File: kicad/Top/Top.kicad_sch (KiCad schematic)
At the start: 1 part

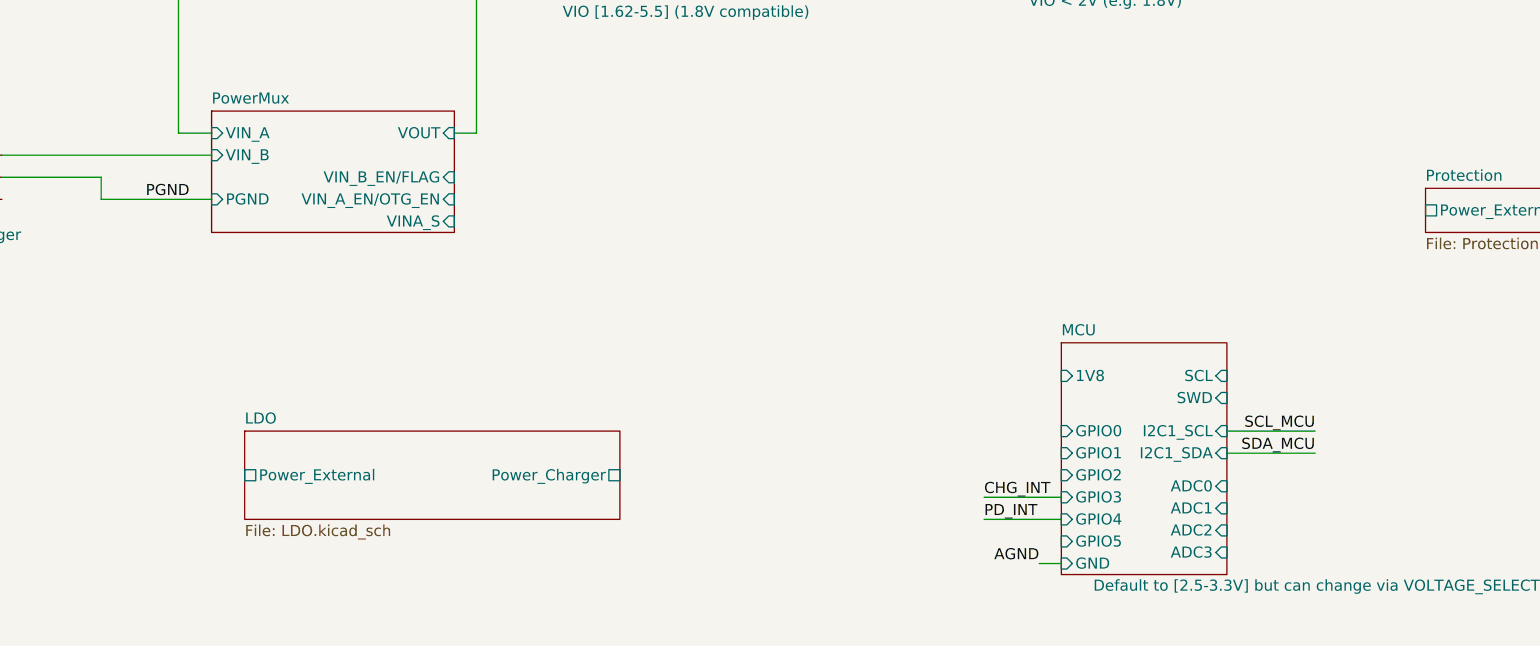
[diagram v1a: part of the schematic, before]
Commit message: Wired up power mux MCU interfaces
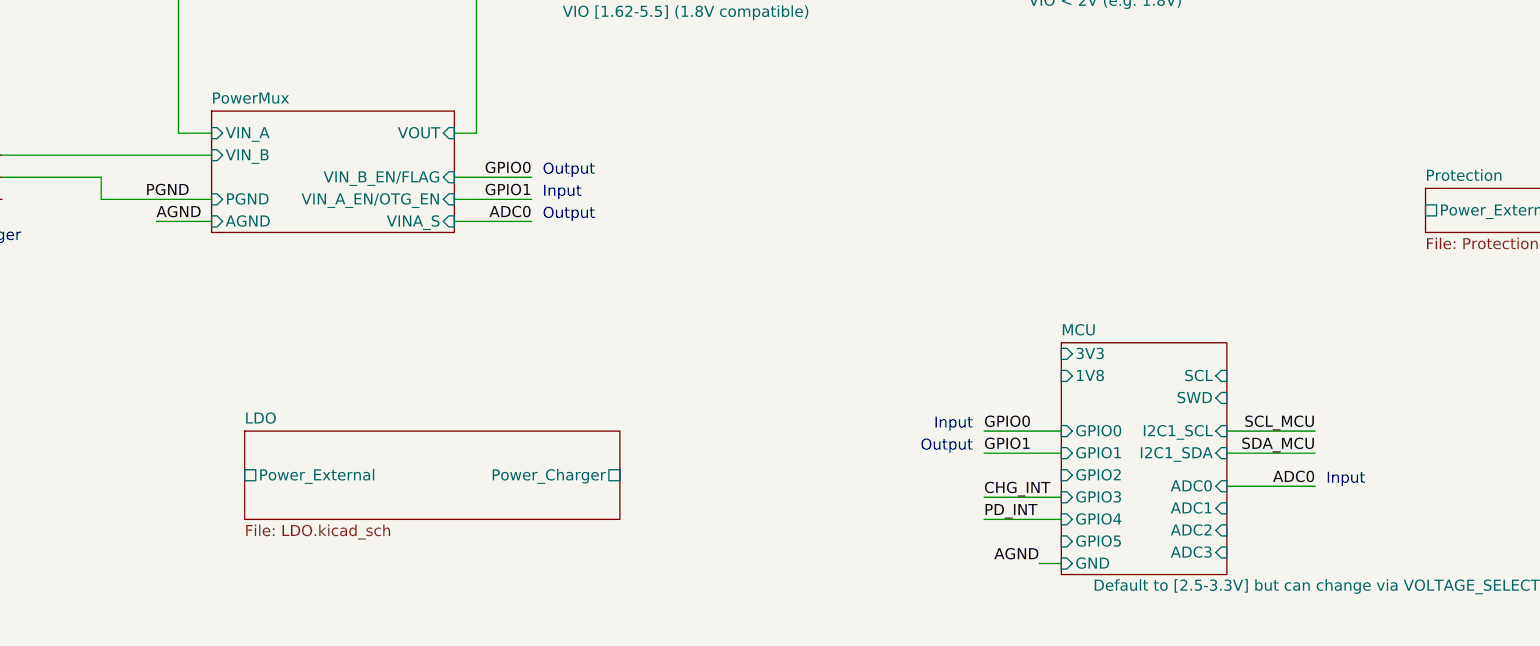
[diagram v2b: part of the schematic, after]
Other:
- sheet MCU ports: added 3V3; removed none
- sheet PowerMux ports: added AGND; removed none
- note added: "Input"
- note added: "Output"
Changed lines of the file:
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@@
+    (stroke (width 0) (type default) (color 0 0 0 0))
+  )
+  (wire (pts (xy 127 87.63) (xy 135.89 87.63))
+    (stroke (width 0) (type default) (color 0 0 0 0))
+  )
+  (wire (pts (xy 135.89 82.55) (xy 127 82.55))
+    (stroke (width 0) (type default) (color 0 0 0 0))
+  )
+  (wire (pts (xy 215.9 118.11) (xy 226.06 118.11))
     (stroke (width 0) (type default) (color 0 0 0 0))
   )
@@
     (stroke (width 0) (type default) (color 0 0 0 0))
   )
+  (wire (pts (xy 99.06 87.63) (xy 92.71 87.63))
+    (stroke (width 0) (type default) (color 0 0 0 0))
+  )
   (wire (pts (xy 160.02 48.26) (xy 168.91 48.26))
     (stroke (width 0) (type default) (color 0 0 0 0))
@@
     (stroke (width 0) (type default) (color 0 0 0 0))
   )
+  (wire (pts (xy 187.96 111.76) (xy 196.85 111.76))
+    (stroke (width 0) (type default) (color 0 0 0 0))
+  )
   (wire (pts (xy 72.39 21.59) (xy 77.47 21.59))
     (stroke (width 0) (type default) (color 0 0 0 0))
@@
     (stroke (width 0) (type default) (color 0 0 0 0))
   )
+  (wire (pts (xy 187.96 114.3) (xy 196.85 114.3))
+    (stroke (width 0) (type default) (color 0 0 0 0))
+  )
   (wire (pts (xy 129.54 77.47) (xy 129.54 34.29))
     (stroke (width 0) (type default) (color 0 0 0 0))
@@
   )
   (wire (pts (xy 185.42 40.64) (xy 191.77 40.64))
+    (stroke (width 0) (type default) (color 0 0 0 0))
+  )
+  (wire (pts (xy 135.89 85.09) (xy 127 85.09))
     (stroke (width 0) (type default) (color 0 0 0 0))
   )
@@
     (effects (font (size 1.27 1.27)) (justify left bottom))
   )
+  (text "Input" (at 186.69 111.76 180)
+    (effects (font (size 1.27 1.27)) (justify right bottom))
+  )
+  (text "Output" (at 137.16 82.55 0)
+    (effects (font (size 1.27 1.27)) (justify left bottom))
+  )
+  (text "Input" (at 137.16 85.09 0)
+    (effects (font (size 1.27 1.27)) (justify left bottom))
+  )
+  (text "Output" (at 137.16 87.63 0)
+    (effects (font (size 1.27 1.27)) (justify left bottom))
+  )
+  (text "Output" (at 186.69 114.3 180)
+    (effects (font (size 1.27 1.27)) (justify right bottom))
+  )
+  (text "Input" (at 227.33 118.11 0)
+    (effects (font (size 1.27 1.27)) (justify left bottom))
+  )
   (label "CHG_INT" (at 187.96 119.38 0)
     (effects (font (size 1.27 1.27)) (justify left bottom))
@@
     (effects (font (size 1.27 1.27)) (justify left bottom))
   )
+  (label "AGND" (at 92.71 87.63 0)
+    (effects (font (size 1.27 1.27)) (justify left bottom))
+  )
   (label "1.8V" (at 78.74 48.26 180)
     (effects (font (size 1.27 1.27)) (justify right bottom))
@@
     (effects (font (size 1.27 1.27)) (justify right bottom))
   )
+  (label "GPIO1" (at 135.89 85.09 180)
+    (effects (font (size 1.27 1.27)) (justify right bottom))
+  )
+  (label "GPIO0" (at 135.89 82.55 180)
+    (effects (font (size 1.27 1.27)) (justify right bottom))
+  )
+  (label "GPIO1" (at 187.96 114.3 0)
+    (effects (font (size 1.27 1.27)) (justify left bottom))
+  )
   (label "SDA_MCU" (at 226.06 114.3 180)
     (effects (font (size 1.27 1.27)) (justify right bottom))
@@
     (effects (font (size 1.27 1.27)) (justify right bottom))
   )
+  (label "ADC0" (at 135.89 87.63 180)
+    (effects (font (size 1.27 1.27)) (justify right bottom))
+  )
   (label "SDA_PD" (at 81.28 53.34 180)
     (effects (font (size 1.27 1.27)) (justify right bottom))
@@
   (label "AGND" (at 166.37 54.61 180)
     (effects (font (size 1.27 1.27)) (justify right bottom))
+  )
+  (label "ADC0" (at 226.06 118.11 180)
+    (effects (font (size 1.27 1.27)) (justify right bottom))
+  )
+  (label "GPIO0" (at 187.96 111.76 0)
+    (effects (font (size 1.27 1.27)) (justify left bottom))
   )
   (label "SYS" (at 77.47 21.59 180)
@@
       (effects (font (size 1.27 1.27)) (justify right))
     )
+    (pin "3V3" input (at 196.85 102.87 180)
+      (effects (font (size 1.27 1.27)) (justify left))
+    )
   )
   (sheet (at 99.06 74.93) (size 27.94 13.97) (fields_autoplaced)
@@
     (pin "VINA_S" input (at 127 87.63 0)
       (effects (font (size 1.27 1.27)) (justify right))
+    )
+    (pin "AGND" input (at 99.06 87.63 180)
+      (effects (font (size 1.27 1.27)) (justify left))
     )
   )
@@
       (reference "C?") (unit 1) (value "10uF") (footprint "")
     )
+    (path "/b17a9dbb-4562-473a-b13f-bbad723355f8/4807e2b0-3f60-4d41-a0cc-ee902e81d7ab"
+      (reference "C?") (unit 1) (value "100n") (footprint "Capacitor_SMD:C_0402_1005Metric")
+    )
     (path "/3b7e5198-fb12-4059-9002-c176f652e784/4c953f3a-dc40-4122-89b2-145f82abc098"
       (reference "C?") (unit 1) (value "0.1uF") (footprint "")
@@
       (reference "C?") (unit 1) (value "10nF") (footprint "")
     )
+    (path "/b17a9dbb-4562-473a-b13f-bbad723355f8/ea0eb13f-7d93-496c-b4f9-195da6a28f8d"
+      (reference "C?") (unit 1) (value "100n") (footprint "Capacitor_SMD:C_0402_1005Metric")
+    )
     (path "/3b7e5198-fb12-4059-9002-c176f652e784/f147c89c-1eb3-4bed-90e8-126acad15e7d"
       (reference "C?") (unit 1) (value "DNP") (footprint "")
@@
       (reference "R65") (unit 1) (value "R_SEN") (footprint "AltiumImports:1206")
     )
+    (path "/e17fda7c-211f-4188-9d42-b948f78009dd/0cea1315-6c66-4c7d-babe-09dc48335b98"
+      (reference "R?") (unit 1) (value "4.64M") (footprint "")
+    )
     (path "/b17a9dbb-4562-473a-b13f-bbad723355f8/19d6e89f-5af0-4248-ad27-14f3cf2d11c3"
       (reference "R?") (unit 1) (value "1") (footprint "")
@@
       (reference "R?") (unit 1) (value "1") (footprint "")
     )
+    (path "/e17fda7c-211f-4188-9d42-b948f78009dd/fb5ff5e7-45b6-4903-ab08-36293b183844"
+      (reference "R?") (unit 1) (value "2.61M") (footprint "")
+    )
     (path "/427922e5-a943-4728-8788-709c0c3b2395/5348c353-2ef7-4ba8-ba47-d79055695ce1"

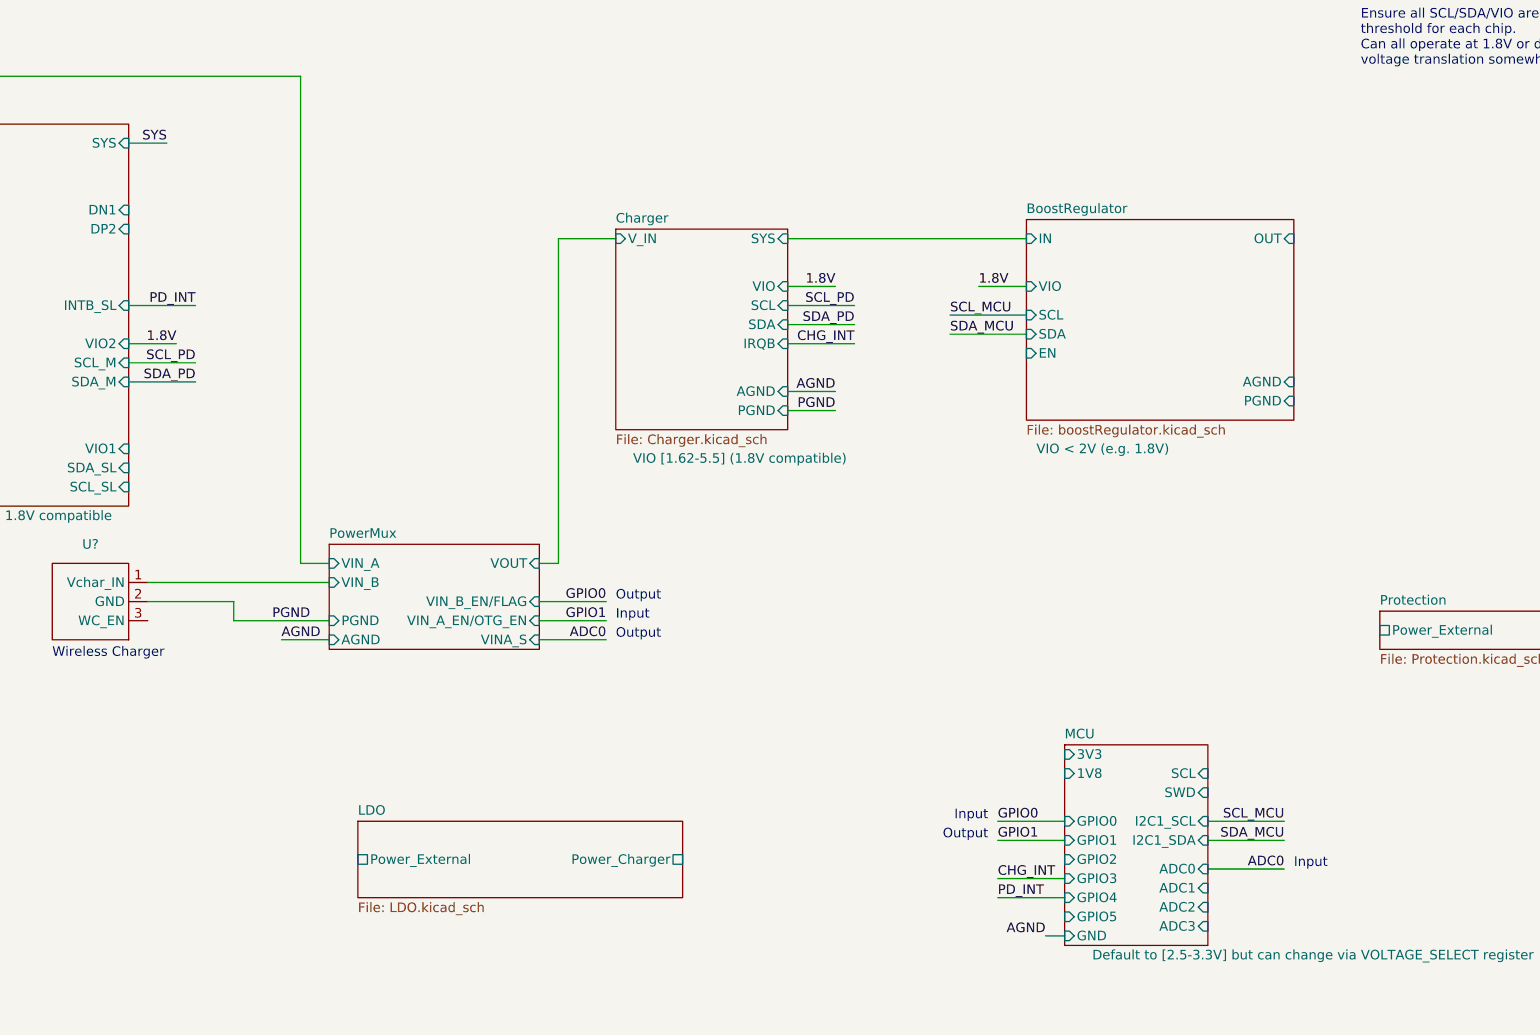
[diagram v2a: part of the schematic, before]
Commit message: Moved GND merge to top sheet
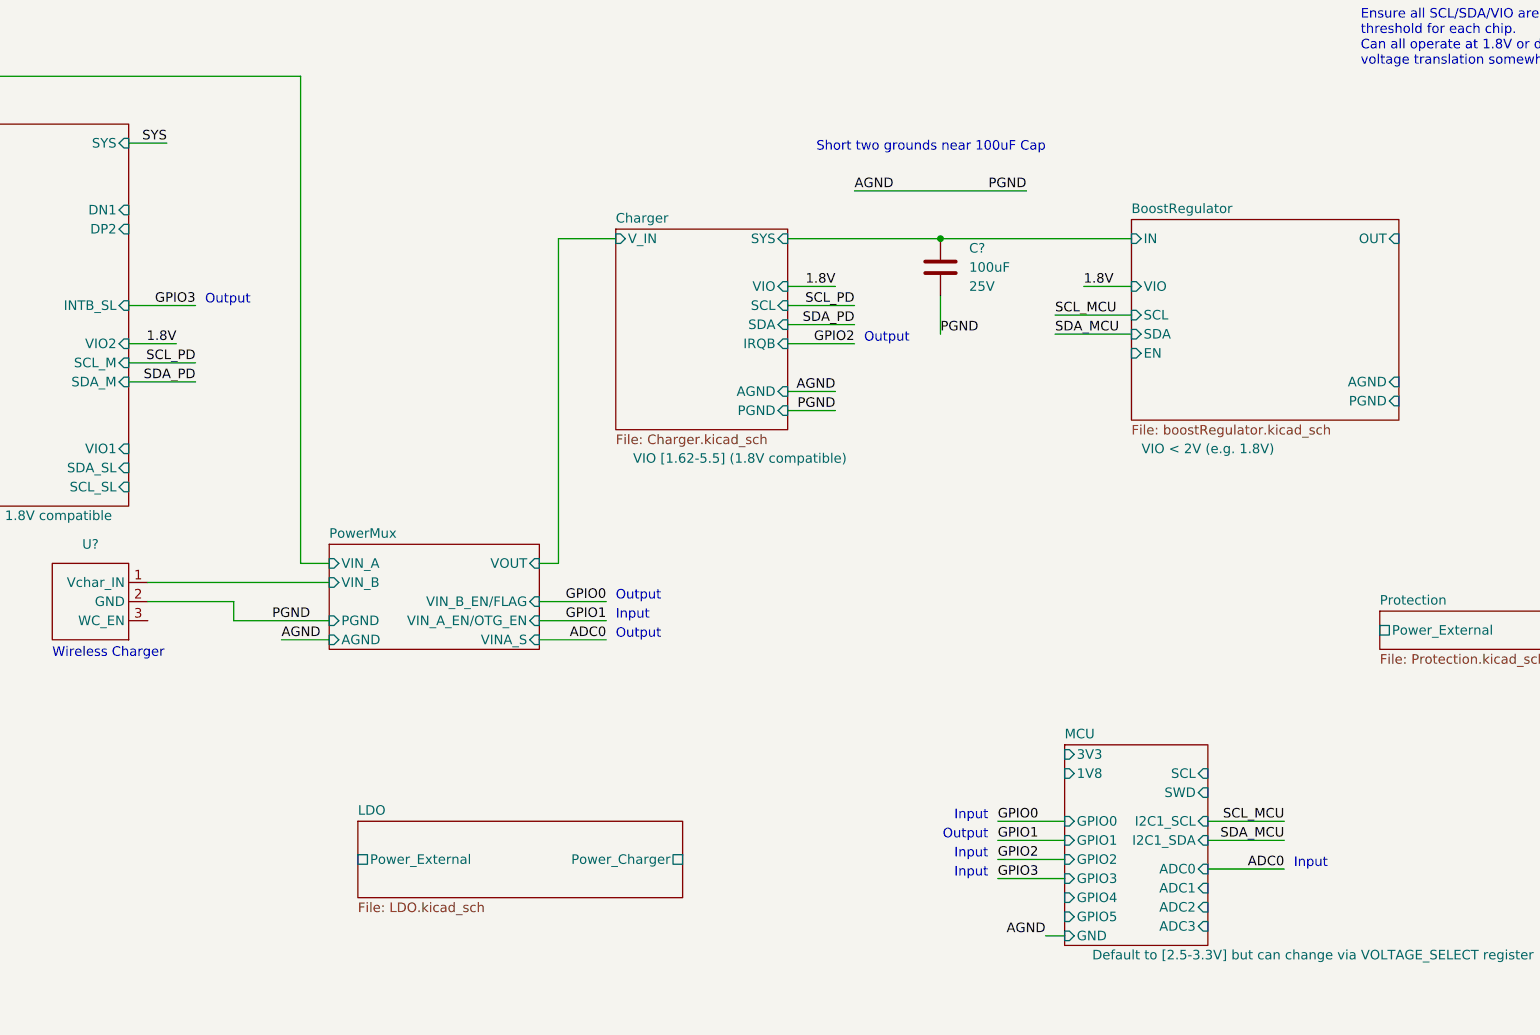
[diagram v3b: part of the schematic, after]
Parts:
- added C?: 100uF, symbol Device:C
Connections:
- net PGND is gone; now on net AGND: U?.2 (GND)
- net AGND: now also C?.2
- net BoostRegulator/IN: now also C?.1
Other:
- note added: "Short two grounds near 100uF Cap"
